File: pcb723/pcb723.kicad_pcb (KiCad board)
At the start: 4 copper layers, 57 parts, among them J1 Conn_01x02_Pin, J2 Conn_01x02_Pin, J3 Conn_02x07_Odd_Even, J4 Conn_02x04_Odd_Even, J5 USB_C_Receptacle_USB2.0_16P, SW1 SW_Push, U1 STM32H723ZGT6, U2 AMS1117-3.3, Y1 8MHz 20pF

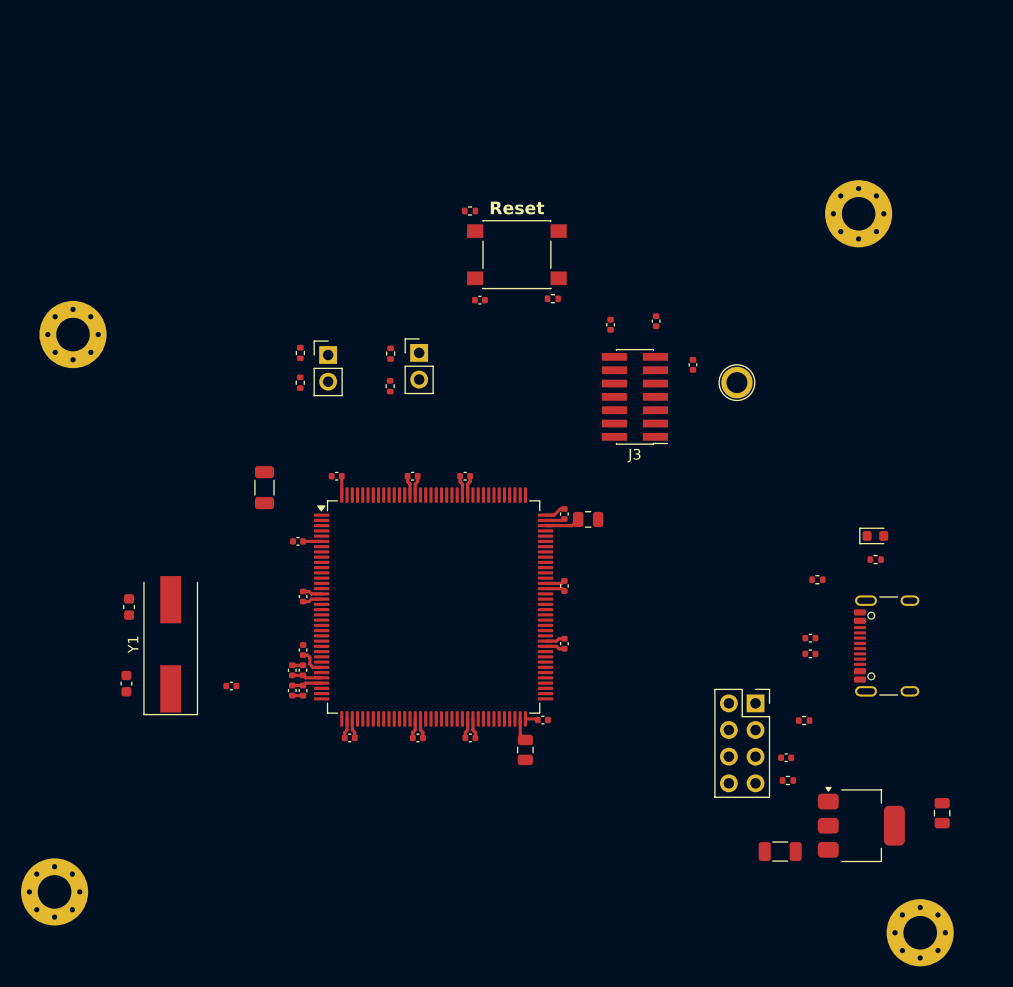
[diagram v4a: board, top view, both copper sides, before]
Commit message: Connect external crystal clock
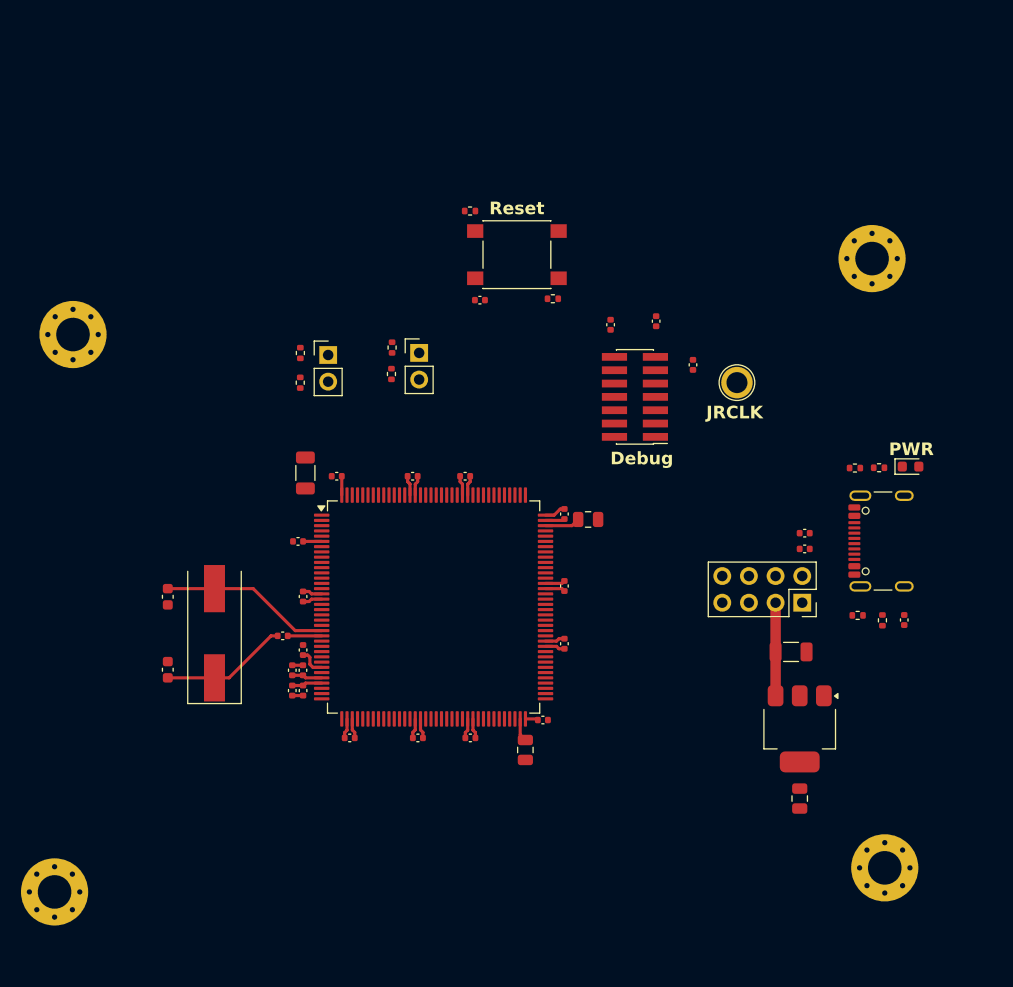
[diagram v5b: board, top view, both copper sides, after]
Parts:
- moved C25 19.0 mm to (160.9, 83.0), turned to 0 degrees
- moved R13 17.7 mm to (169.6, 80.0), turned to -90 degrees
- moved C26 17.3 mm to (171.7, 80.0), turned to 90 degrees
- moved C24 13.6 mm to (161.7, 97.0), turned to -90 degrees
- moved R11 11.2 mm to (167.2, 79.5)
- moved R12 11.2 mm to (167.0, 65.5)
- moved U2 10.9 mm to (161.7, 90.4), turned to -90 degrees
- moved J4 10.6 mm to (162.0, 78.3), turned to -90 degrees
- moved J5 10.0 mm to (170.6, 72.5)
- moved R15 10.0 mm to (162.2, 73.2)
- moved R16 10.0 mm to (162.2, 71.7)
- moved R14 8.76 mm to (169.3, 65.5)
- moved D1 7.41 mm to (172.3, 65.4)
- moved H4 7.04 mm to (169.8, 103.6)
- moved R7 6.84 mm to (112.5, 81.5)
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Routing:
- net /PH0: track 0.00 -> 16.3 mm
- net Net-(C22-Pad1): track 0.00 -> 12.1 mm
- net Net-(J4-Pin_1): track 0.00 -> 8.87 mm
- net /PH1: track 0.00 -> 3.23 mm
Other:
- board text added: "Debug"
- board text added: "JRCLK"
- board text added: "PWR"

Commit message: Add 26 pin breakout
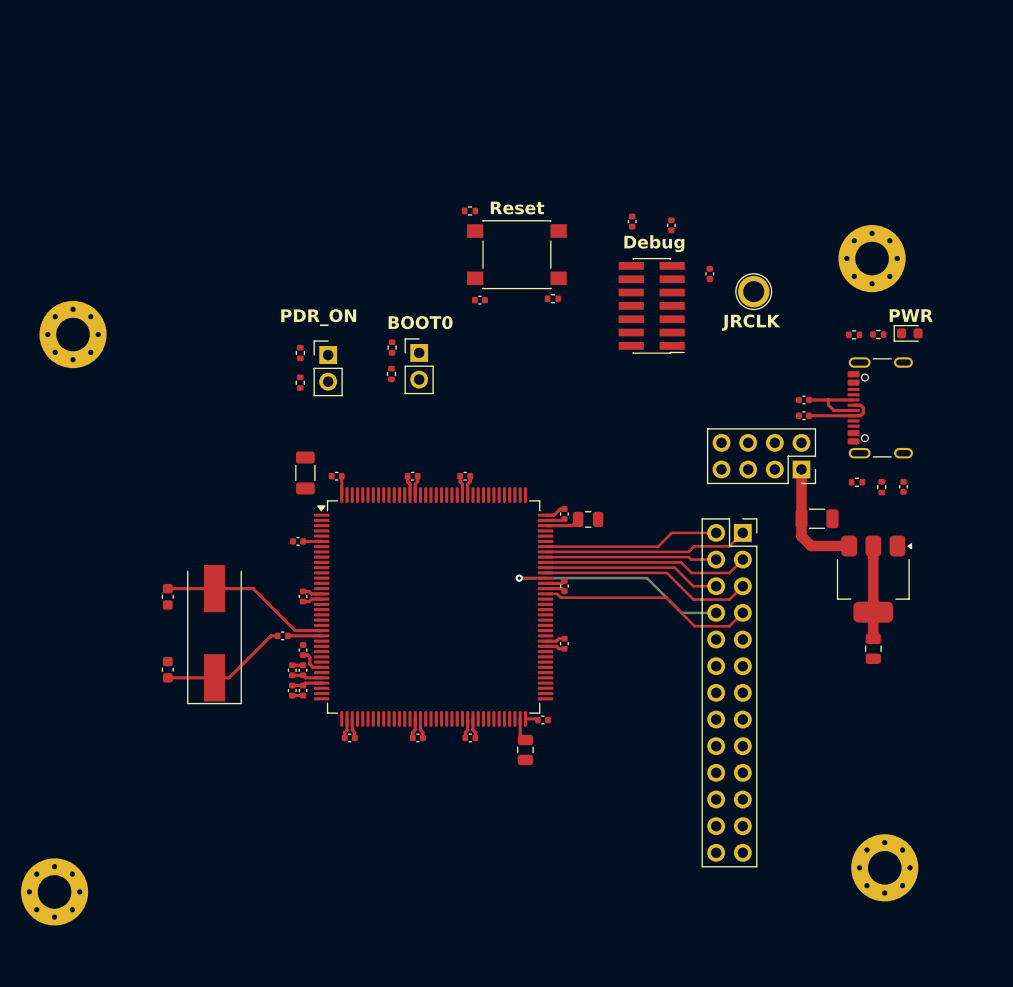
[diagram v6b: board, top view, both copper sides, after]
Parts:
- added J6: Conn_02x13_Odd_Even, Connector_PinSocket_2.54mm:PinSocket_2x13_P2.54mm_Vertical, F.Cu at (156.3, 71.7)
- moved C24 15.9 mm to (168.7, 82.7)
- moved U2 15.9 mm to (168.7, 76.1)
- moved C25 12.9 mm to (163.4, 70.3)
- moved D1 12.7 mm to (172.2, 52.7)
- moved J5 12.7 mm to (170.5, 59.8)
- moved R12 12.7 mm to (166.9, 52.8)
- moved R14 12.7 mm to (169.2, 52.8)
- moved R15 12.7 mm to (162.1, 60.5), turned to 180 degrees
- moved R16 12.7 mm to (162.1, 59.0), turned to 180 degrees
- moved C26 12.7 mm to (171.6, 67.3)
- moved J4 12.7 mm to (161.9, 65.7)
- moved R11 12.7 mm to (167.2, 66.9)
- moved R13 12.7 mm to (169.5, 67.3)
- moved R9 10.0 mm to (145.8, 42.0)
- moved R10 9.25 mm to (149.5, 42.4)
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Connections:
- U1 pad 100: unconnected-(U1-PA8-Pad100) -> /PA8
- U1 pad 101: unconnected-(U1-PA9-Pad101) -> /PA9
- U1 pad 102: unconnected-(U1-PA10-Pad102) -> /PA10
- U1 pad 93: unconnected-(U1-PG8-Pad93) -> /PG8
- U1 pad 96: unconnected-(U1-PC6-Pad96) -> /PC6
- U1 pad 97: unconnected-(U1-PC7-Pad97) -> /PC7
- U1 pad 98: unconnected-(U1-PC8-Pad98) -> /PC8
- U1 pad 99: unconnected-(U1-PC9-Pad99) -> /PC9
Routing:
- net /PC6: track 0.00 -> 22.6 mm, vias 0 -> 1
- net /PG8: track 0.00 -> 20.6 mm
- net /PC7: track 0.00 -> 20.4 mm
- net /PC9: track 0.00 -> 19.7 mm
- net /PA9: track 0.00 -> 19.5 mm
- net /PC8: track 0.00 -> 17.0 mm
- net /PA10: track 0.00 -> 16.8 mm
- net /PA8: track 0.00 -> 16.4 mm
- net +3V3: track 30.5 -> 39.3 mm
- net Net-(J5-D+-PadA6): track 0.00 -> 7.35 mm
- net Net-(J5-D--PadA7): track 0.00 -> 6.81 mm
- net Net-(J4-Pin_1): track 8.87 -> 11.3 mm
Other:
- board text added: "BOOT0"
- board text added: "PDR_ON"

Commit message: Connect starting breakout pins
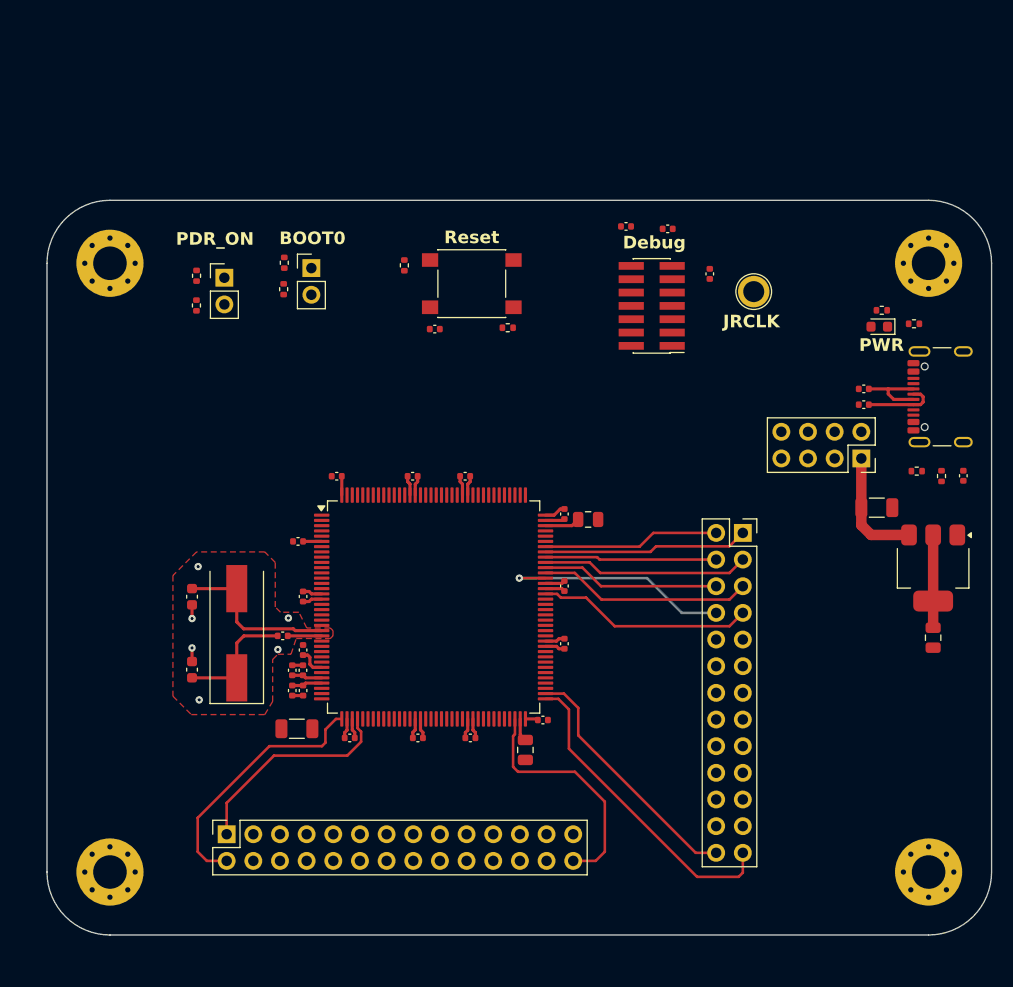
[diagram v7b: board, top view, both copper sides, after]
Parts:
- added J7: Conn_02x14_Odd_Even, Connector_PinSocket_2.54mm:PinSocket_2x14_P2.54mm_Vertical, F.Cu at (107.1, 100.4)
- moved C18 24.4 mm to (113.8, 90.3), turned to 180 degrees
- moved J1 13.1 mm to (115.2, 46.5)
- moved R1 13.1 mm to (112.5, 48.5)
- moved R2 13.1 mm to (112.6, 46.0)
- moved J2 12.3 mm to (106.9, 47.4)
- moved R3 12.3 mm to (104.2, 50.0)
- moved R4 12.3 mm to (104.2, 47.2)
- moved R6 8.13 mm to (124.0, 46.2), turned to -90 degrees
- moved H1 7.65 mm to (96.0, 46.0)
- moved C24 5.80 mm to (174.4, 81.7)
- moved J4 5.80 mm to (167.6, 64.6)
- moved U2 5.80 mm to (174.4, 75.0)
- moved J5 5.80 mm to (176.2, 58.7)
- moved R12 5.80 mm to (172.6, 51.8)
- moved R11 5.80 mm to (172.9, 65.8)
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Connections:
- J6 pad 10: unconnected-(J6-Pin_10-Pad10) -> /PG7
- J6 pad 11: unconnected-(J6-Pin_11-Pad11) -> /PG4
- J6 pad 12: unconnected-(J6-Pin_12-Pad12) -> /PG5
- J6 pad 13: unconnected-(J6-Pin_13-Pad13) -> /PG2
- J6 pad 14: unconnected-(J6-Pin_14-Pad14) -> /PG3
- J6 pad 15: unconnected-(J6-Pin_15-Pad15) -> /PD14
- J6 pad 16: unconnected-(J6-Pin_16-Pad16) -> /PD15
- J6 pad 17: unconnected-(J6-Pin_17-Pad17) -> /PD12
- J6 pad 18: unconnected-(J6-Pin_18-Pad18) -> /PD13
- J6 pad 19: unconnected-(J6-Pin_19-Pad19) -> /PD10
- J6 pad 20: unconnected-(J6-Pin_20-Pad20) -> /PD11
- J6 pad 21: unconnected-(J6-Pin_21-Pad21) -> /PD8
- J6 pad 22: unconnected-(J6-Pin_22-Pad22) -> /PD9
- J6 pad 23: unconnected-(J6-Pin_23-Pad23) -> /PB14
- J6 pad 24: unconnected-(J6-Pin_24-Pad24) -> /PB15
- J6 pad 25: unconnected-(J6-Pin_25-Pad25) -> /PB12
- J6 pad 26: unconnected-(J6-Pin_26-Pad26) -> /PB13
- J6 pad 9: unconnected-(J6-Pin_9-Pad9) -> /PG6
- U1 pad 37: unconnected-(U1-PA3-Pad37) -> /PA3
- U1 pad 40: unconnected-(U1-PA4-Pad40) -> /PA4
- U1 pad 70: unconnected-(U1-PB11-Pad70) -> /PB11
- U1 pad 73: unconnected-(U1-PB12-Pad73) -> /PB12
- U1 pad 74: unconnected-(U1-PB13-Pad74) -> /PB13
- U1 pad 75: unconnected-(U1-PB14-Pad75) -> /PB14
- U1 pad 76: unconnected-(U1-PB15-Pad76) -> /PB15
- U1 pad 77: unconnected-(U1-PD8-Pad77) -> /PD8
- U1 pad 78: unconnected-(U1-PD9-Pad78) -> /PD9
- U1 pad 79: unconnected-(U1-PD10-Pad79) -> /PD10
- U1 pad 80: unconnected-(U1-PD11-Pad80) -> /PD11
- U1 pad 81: unconnected-(U1-PD12-Pad81) -> /PD12
- U1 pad 82: unconnected-(U1-PD13-Pad82) -> /PD13
- U1 pad 85: unconnected-(U1-PD14-Pad85) -> /PD14
- U1 pad 86: unconnected-(U1-PD15-Pad86) -> /PD15
- U1 pad 87: unconnected-(U1-PG2-Pad87) -> /PG2
- U1 pad 88: unconnected-(U1-PG3-Pad88) -> /PG3
- U1 pad 89: unconnected-(U1-PG4-Pad89) -> /PG4
- U1 pad 90: unconnected-(U1-PG5-Pad90) -> /PG5
- U1 pad 91: unconnected-(U1-PG6-Pad91) -> /PG6
- U1 pad 92: unconnected-(U1-PG7-Pad92) -> /PG7
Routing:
- net /PB12: track 0.00 -> 30.1 mm
- net /PA3: track 0.00 -> 24.7 mm
- net /PB13: track 0.00 -> 24.1 mm
- net /PB11: track 0.00 -> 22.9 mm
- net /PA4: track 0.00 -> 20.5 mm
- net GND: track 19.1 -> 21.7 mm, vias 0 -> 6
- added copper zone on In2.Cu, net +3V3
- added copper zone on F.Cu, net GND
- added copper zone on In1.Cu, net GND
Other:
- board outline added: 90 x 70 mm

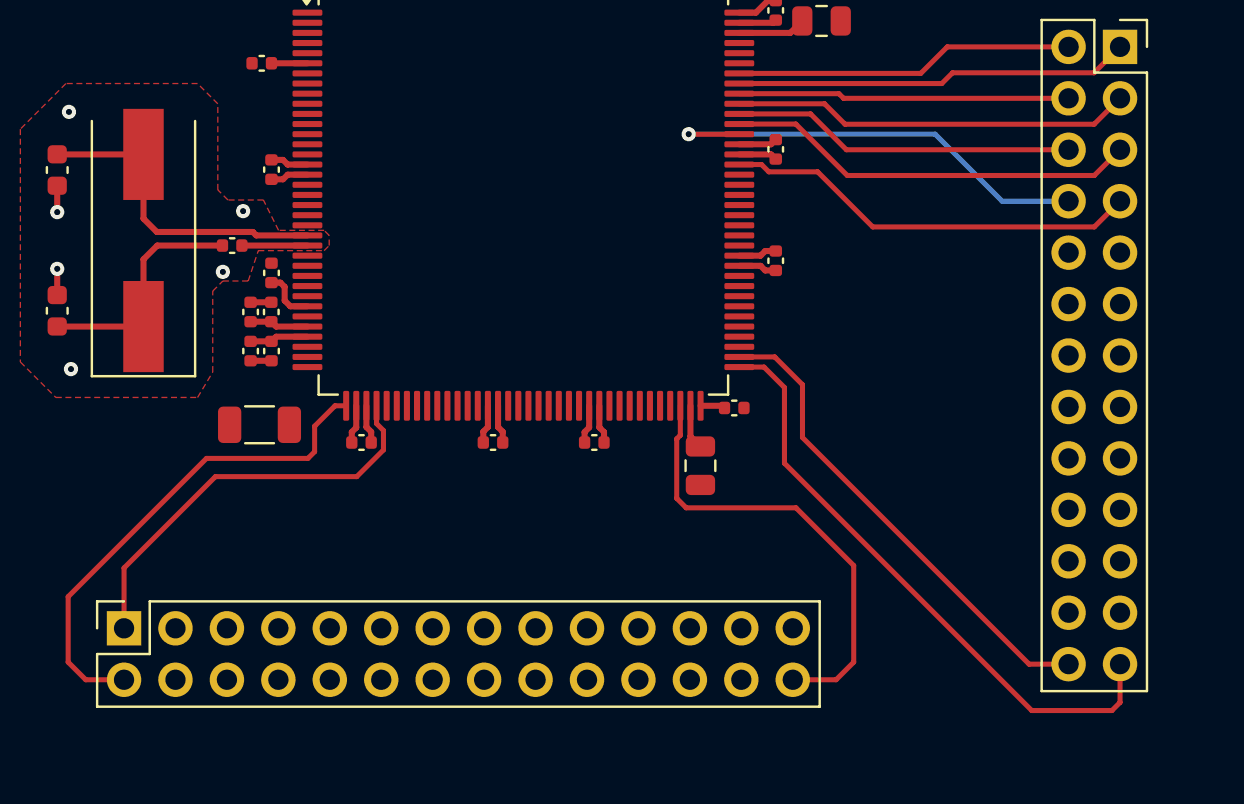
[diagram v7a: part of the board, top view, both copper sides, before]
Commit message: Connect 28-pin socket header
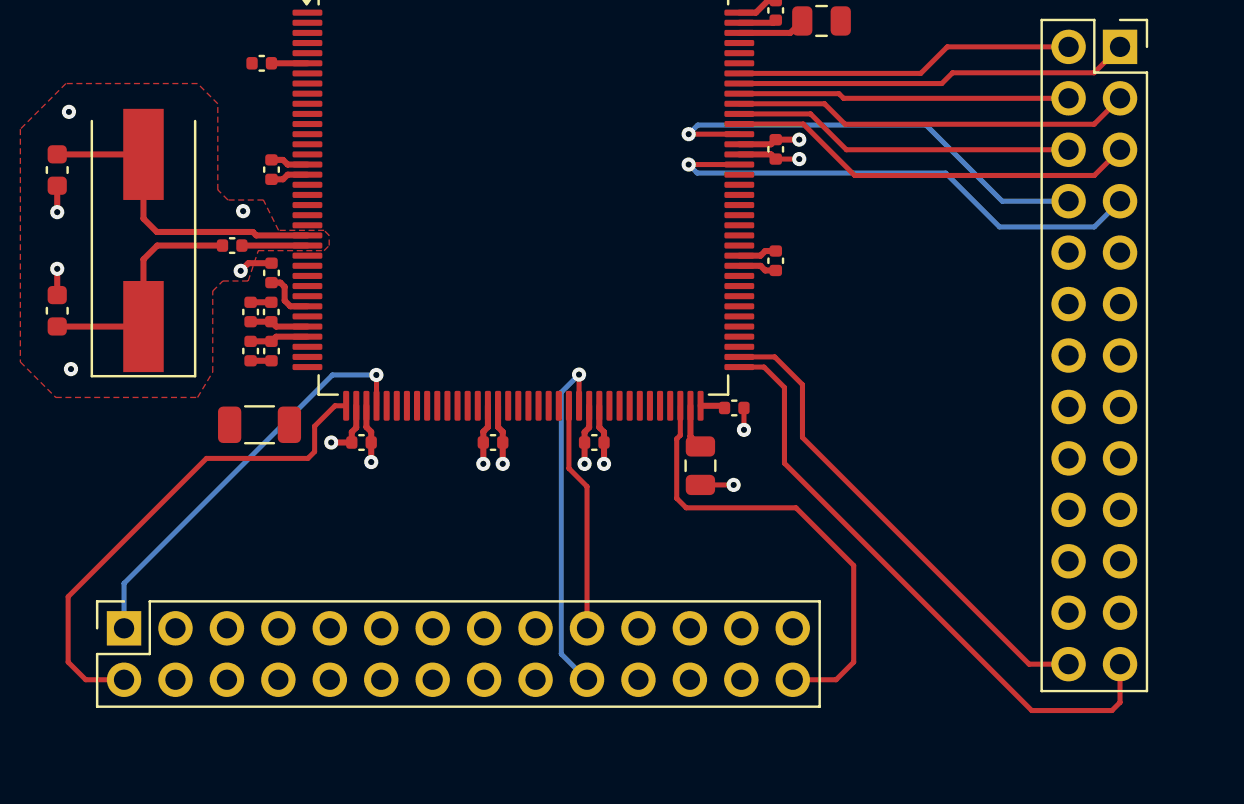
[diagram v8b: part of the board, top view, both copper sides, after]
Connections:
- J7 pad 10: unconnected-(J7-Pin_10-Pad10) -> /PB2
- J7 pad 11: unconnected-(J7-Pin_11-Pad11) -> /PF11
- J7 pad 12: unconnected-(J7-Pin_12-Pad12) -> /PF12
- J7 pad 13: unconnected-(J7-Pin_13-Pad13) -> /PF13
- J7 pad 14: unconnected-(J7-Pin_14-Pad14) -> /PF14
- J7 pad 15: unconnected-(J7-Pin_15-Pad15) -> /PF15
- J7 pad 16: unconnected-(J7-Pin_16-Pad16) -> /PG0
- J7 pad 17: unconnected-(J7-Pin_17-Pad17) -> /PG1
- J7 pad 18: unconnected-(J7-Pin_18-Pad18) -> /PE7
- J7 pad 19: unconnected-(J7-Pin_19-Pad19) -> /PE8
- J7 pad 20: unconnected-(J7-Pin_20-Pad20) -> /PE9
- J7 pad 21: unconnected-(J7-Pin_21-Pad21) -> /PE11
- J7 pad 22: unconnected-(J7-Pin_22-Pad22) -> /PE10
- J7 pad 23: unconnected-(J7-Pin_23-Pad23) -> /PE13
- J7 pad 24: unconnected-(J7-Pin_24-Pad24) -> /PE12
- J7 pad 25: unconnected-(J7-Pin_25-Pad25) -> /PE15
- J7 pad 26: unconnected-(J7-Pin_26-Pad26) -> /PE14
- J7 pad 27: unconnected-(J7-Pin_27-Pad27) -> /PB10
- J7 pad 3: unconnected-(J7-Pin_3-Pad3) -> /PA5
- J7 pad 4: unconnected-(J7-Pin_4-Pad4) -> /PA6
- J7 pad 5: unconnected-(J7-Pin_5-Pad5) -> /PA7
- J7 pad 6: unconnected-(J7-Pin_6-Pad6) -> /PC4
- J7 pad 7: unconnected-(J7-Pin_7-Pad7) -> /PC5
- J7 pad 8: unconnected-(J7-Pin_8-Pad8) -> /PB0
- J7 pad 9: unconnected-(J7-Pin_9-Pad9) -> /PB1
- U1 pad 41: unconnected-(U1-PA5-Pad41) -> /PA5
- U1 pad 42: unconnected-(U1-PA6-Pad42) -> /PA6
- U1 pad 43: unconnected-(U1-PA7-Pad43) -> /PA7
- U1 pad 44: unconnected-(U1-PC4-Pad44) -> /PC4
- U1 pad 45: unconnected-(U1-PC5-Pad45) -> /PC5
- U1 pad 46: unconnected-(U1-PB0-Pad46) -> /PB0
- U1 pad 47: unconnected-(U1-PB1-Pad47) -> /PB1
- U1 pad 48: unconnected-(U1-PB2-Pad48) -> /PB2
- U1 pad 49: unconnected-(U1-PF11-Pad49) -> /PF11
- U1 pad 50: unconnected-(U1-PF12-Pad50) -> /PF12
- U1 pad 53: unconnected-(U1-PF13-Pad53) -> /PF13
- U1 pad 54: unconnected-(U1-PF14-Pad54) -> /PF14
- U1 pad 55: unconnected-(U1-PF15-Pad55) -> /PF15
- U1 pad 56: unconnected-(U1-PG0-Pad56) -> /PG0
- U1 pad 57: unconnected-(U1-PG1-Pad57) -> /PG1
- U1 pad 58: unconnected-(U1-PE7-Pad58) -> /PE7
- U1 pad 59: unconnected-(U1-PE8-Pad59) -> /PE8
- U1 pad 60: unconnected-(U1-PE9-Pad60) -> /PE9
- U1 pad 63: unconnected-(U1-PE10-Pad63) -> /PE10
- U1 pad 64: unconnected-(U1-PE11-Pad64) -> /PE11
- U1 pad 65: unconnected-(U1-PE12-Pad65) -> /PE12
- U1 pad 66: unconnected-(U1-PE13-Pad66) -> /PE13
- U1 pad 67: unconnected-(U1-PE14-Pad67) -> /PE14
- U1 pad 68: unconnected-(U1-PE15-Pad68) -> /PE15
- U1 pad 69: unconnected-(U1-PB10-Pad69) -> /PB10
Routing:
- net /PE9: track 0.00 -> 17.5 mm, vias 0 -> 1
- net /PE8: track 0.00 -> 11.4 mm
- net GND: track 21.7 -> 30.4 mm, vias 6 -> 12
- net /PG8: track 20.6 -> 25.6 mm, vias 0 -> 1
- net +3V3: track 39.3 -> 43.5 mm, vias 0 -> 4
- net /PA4: vias 0 -> 1
